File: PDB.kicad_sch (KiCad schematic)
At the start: 42 parts, among them J101 Conn_01x02_Female, J102 Conn_01x08_Female, J103 Conn_01x08_Female, J104 Conn_01x06_Female, U101 AZ1084-3.3, U102 MCP2562-H-SN, U103 AZ1117-5.0, U104 INA180, U105 STM32F103C8T6, Y101 8MHz

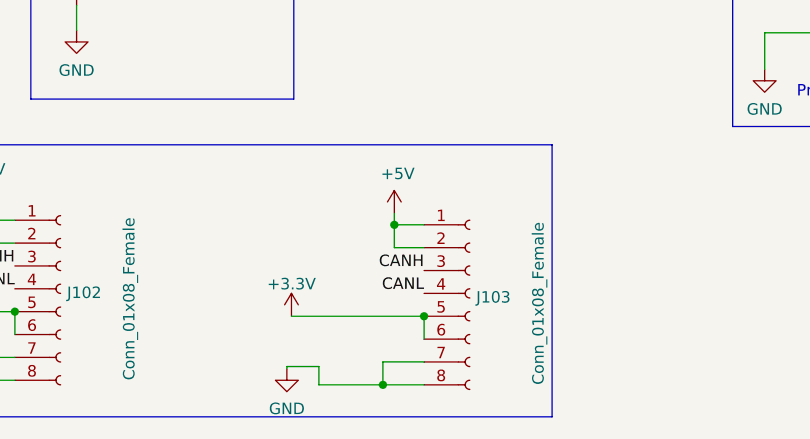
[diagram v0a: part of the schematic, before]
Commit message: placed componets for routing
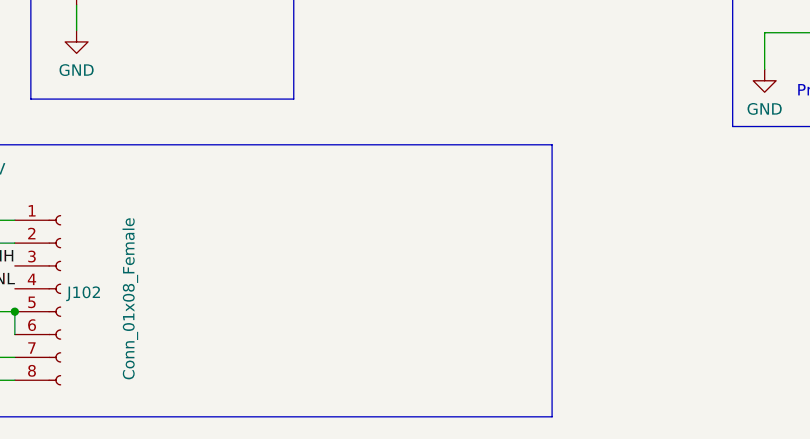
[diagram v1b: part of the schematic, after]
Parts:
- removed J103: Conn_01x08_Female, symbol Connector:Conn_01x08_Female
- C101, C102, C110, C111, C112, C113, C114, C115, C116, C117, C118: footprint Capacitor_SMD:C_0805_2012Metric -> Capacitor_SMD:C_0805_2012Metric_Pad1.18x1.45mm_HandSolder
- C103, C104, C105, C106, C107, C108: footprint (none) -> Capacitor_SMD:C_0805_2012Metric_Pad1.18x1.45mm_HandSolder
- C109: footprint Capacitor_SMD:C_0805_2012Metric_Pad1.15x1.40mm_HandSolder -> Capacitor_SMD:C_0805_2012Metric_Pad1.18x1.45mm_HandSolder
- D102, D103, D104: footprint (none) -> LED_SMD:LED_0805_2012Metric_Pad1.15x1.40mm_HandSolder
- J101: footprint (none) -> Connector_AMASS:AMASS_XT60PW-F_1x02_P7.20mm_Horizontal
- J102: footprint (none) -> Connector_PinHeader_1.27mm:PinHeader_1x08_P1.27mm_Horizontal
- J104: footprint (none) -> Connector:Tag-Connect_TC2030-IDC-FP_2x03_P1.27mm_Vertical
- R101, R103, R104, R105: footprint (none) -> Resistor_SMD:R_0805_2012Metric_Pad1.20x1.40mm_HandSolder
- R102: footprint Resistor_SMD:R_1206_3216Metric_Pad1.42x1.75mm_HandSolder -> Resistor_SMD:R_0805_2012Metric_Pad1.20x1.40mm_HandSolder
- R106, R107: footprint (none) -> Resistor_SMD:R_1206_3216Metric_Pad1.30x1.75mm_HandSolder
- R108: footprint Resistor_SMD:R_0805_2012Metric -> Resistor_SMD:R_0805_2012Metric_Pad1.20x1.40mm_HandSolder

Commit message: changed voltage divider values for voltage measurement
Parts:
- R107: value 1k -> 2k
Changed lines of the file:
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@@
       (effects (font (size 1.27 1.27)) (justify left))
     )
-    (property "Value" "1k" (id 1) (at 123.952 150.0382 0)
+    (property "Value" "2k" (id 1) (at 123.952 150.0382 0)
       (effects (font (size 1.27 1.27)) (justify left))
     )
@@
     )
     (path "/09e834ef-d442-457e-b37f-61ac4fbf53b7"
-      (reference "R107") (unit 1) (value "1k") (footprint "Resistor_SMD:R_1206_3216Metric_Pad1.30x1.75mm_HandSolder")
+      (reference "R107") (unit 1) (value "2k") (footprint "Resistor_SMD:R_1206_3216Metric_Pad1.30x1.75mm_HandSolder")
     )
     (path "/10f93907-8b37-479f-94c5-143e1007e394"
